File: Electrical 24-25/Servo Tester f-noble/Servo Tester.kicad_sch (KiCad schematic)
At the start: 5 parts, among them SW1 RotaryEncoder_Switch, U1 AP2205-33Y-13, U2 ATtiny404-SS, U3 PCF8551ATT_AJ, U4 VIM-878-DP-FC-S-LV

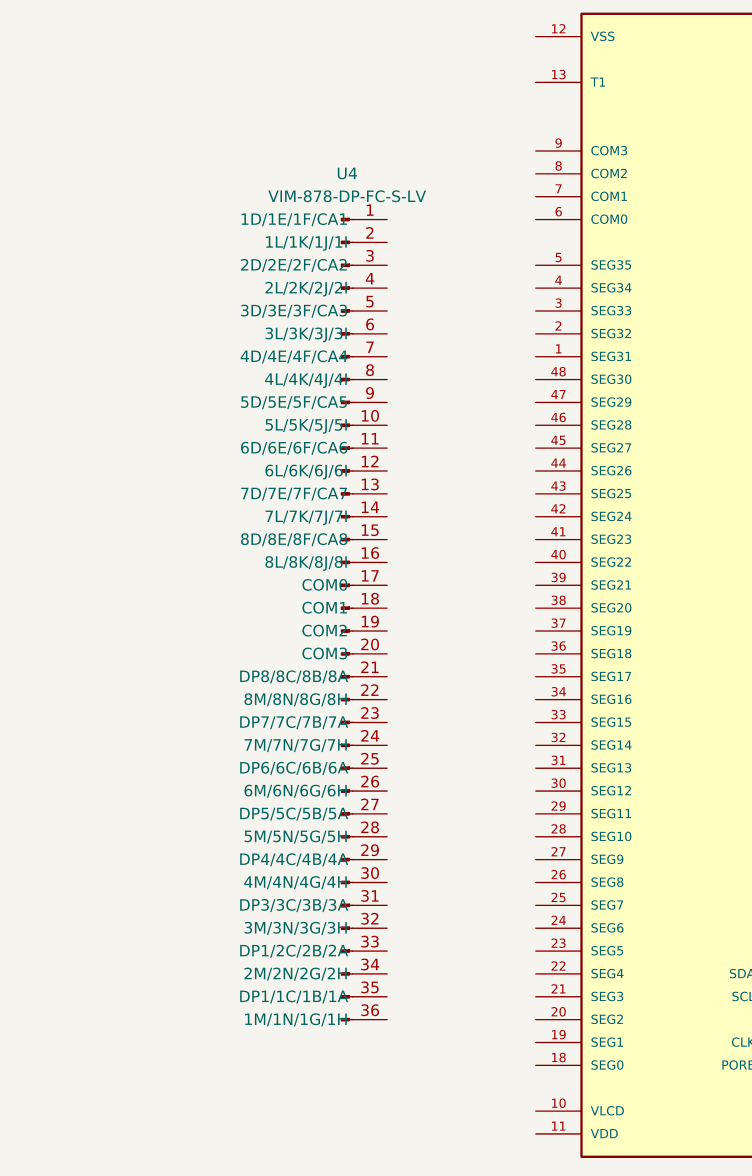
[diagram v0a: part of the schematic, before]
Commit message: added some led wires
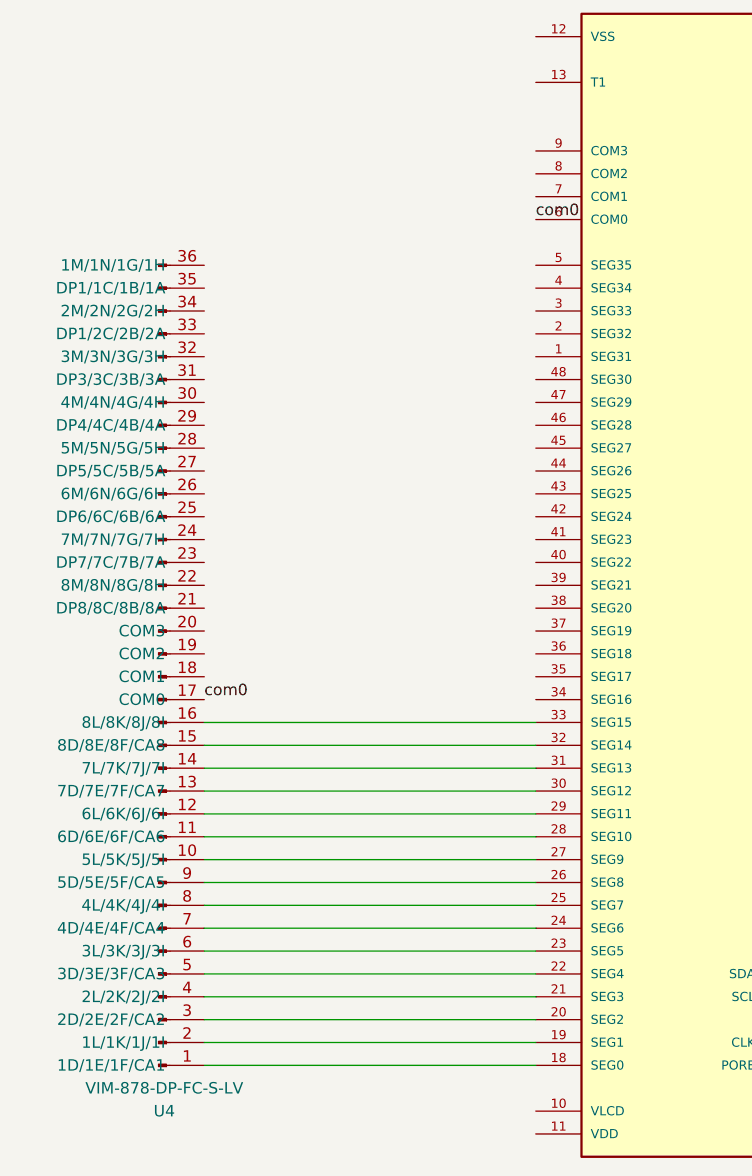
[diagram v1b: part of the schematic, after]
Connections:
- net at U4.1 (1D/1E/1F/CA1): now also U3.18 (SEG0)
- net at U4.10 (5L/5K/5J/5I): now also U3.27 (SEG9)
- net at U4.11 (6D/6E/6F/CA6): now also U3.28 (SEG10)
- net at U4.12 (6L/6K/6J/6I): now also U3.29 (SEG11)
- net at U4.13 (7D/7E/7F/CA7): now also U3.30 (SEG12)
- net at U4.14 (7L/7K/7J/7I): now also U3.31 (SEG13)
- net at U4.15 (8D/8E/8F/CA8): now also U3.32 (SEG14)
- net at U4.16 (8L/8K/8J/8I): now also U3.33 (SEG15)
- net com0: now reaches U4.17 (COM0)
- net com0: now also U3.6 (COM0)
- net at U4.2 (1L/1K/1J/1I): now also U3.19 (SEG1)
- net at U4.3 (2D/2E/2F/CA2): now also U3.20 (SEG2)
- net at U4.4 (2L/2K/2J/2I): now also U3.21 (SEG3)
- net at U4.5 (3D/3E/3F/CA3): now also U3.22 (SEG4)
- net at U4.6 (3L/3K/3J/3I): now also U3.23 (SEG5)
- net at U4.7 (4D/4E/4F/CA4): now also U3.24 (SEG6)
- net at U4.8 (4L/4K/4J/4I): now also U3.25 (SEG7)
- net at U4.9 (5D/5E/5F/CA5): now also U3.26 (SEG8)
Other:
- moved on the sheet: U4
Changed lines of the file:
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@@
+	(wire
+		(pts
+			(xy 34.29 152.4) (xy 71.12 152.4)
+		)
+		(stroke
+			(width 0)
+			(type default)
+		)
+	)
 	(wire
 		(pts
@@
 	(wire
 		(pts
+			(xy 34.29 149.86) (xy 71.12 149.86)
+		)
+		(stroke
+			(width 0)
+			(type default)
+		)
+	)
+	(wire
+		(pts
 			(xy 119.38 81.28) (xy 125.73 81.28)
 		)
@@
 	(wire
 		(pts
+			(xy 34.29 142.24) (xy 71.12 142.24)
+		)
+		(stroke
+			(width 0)
+			(type default)
+		)
+	)
+	(wire
+		(pts
 			(xy 107.95 88.9) (xy 133.35 88.9)
 		)
@@
 	(wire
 		(pts
+			(xy 34.29 165.1) (xy 71.12 165.1)
+		)
+		(stroke
+			(width 0)
+			(type default)
+		)
+	)
+	(wire
+		(pts
 			(xy 140.97 101.6) (xy 133.35 101.6)
 		)
@@
 	(wire
 		(pts
+			(xy 34.29 137.16) (xy 71.12 137.16)
+		)
+		(stroke
+			(width 0)
+			(type default)
+		)
+	)
+	(wire
+		(pts
 			(xy 133.35 148.59) (xy 138.43 148.59)
 		)
@@
 	(wire
 		(pts
+			(xy 34.29 170.18) (xy 71.12 170.18)
+		)
+		(stroke
+			(width 0)
+			(type default)
+		)
+	)
+	(wire
+		(pts
+			(xy 34.29 132.08) (xy 71.12 132.08)
+		)
+		(stroke
+			(width 0)
+			(type default)
+		)
+	)
+	(wire
+		(pts
+			(xy 34.29 162.56) (xy 71.12 162.56)
+		)
+		(stroke
+			(width 0)
+			(type default)
+		)
+	)
+	(wire
+		(pts
+			(xy 34.29 157.48) (xy 71.12 157.48)
+		)
+		(stroke
+			(width 0)
+			(type default)
+		)
+	)
+	(wire
+		(pts
+			(xy 34.29 139.7) (xy 71.12 139.7)
+		)
+		(stroke
+			(width 0)
+			(type default)
+		)
+	)
+	(wire
+		(pts
 			(xy 140.97 81.28) (xy 140.97 101.6)
 		)
@@
 	(wire
 		(pts
+			(xy 34.29 160.02) (xy 71.12 160.02)
+		)
+		(stroke
+			(width 0)
+			(type default)
+		)
+	)
+	(wire
+		(pts
 			(xy 133.35 148.59) (xy 133.35 154.94)
 		)
@@
 	(wire
 		(pts
+			(xy 34.29 167.64) (xy 71.12 167.64)
+		)
+		(stroke
+			(width 0)
+			(type default)
+		)
+	)
+	(wire
+		(pts
+			(xy 34.29 154.94) (xy 71.12 154.94)
+		)
+		(stroke
+			(width 0)
+			(type default)
+		)
+	)
+	(wire
+		(pts
+			(xy 34.29 134.62) (xy 71.12 134.62)
+		)
+		(stroke
+			(width 0)
+			(type default)
+		)
+	)
+	(wire
+		(pts
+			(xy 34.29 144.78) (xy 71.12 144.78)
+		)
+		(stroke
+			(width 0)
+			(type default)
+		)
+	)
+	(wire
+		(pts
 			(xy 119.38 69.85) (xy 119.38 81.28)
 		)
@@
 		)
 	)
-	(label "-VBATT"
-		(at 138.43 148.59 0)
+	(wire
+		(pts
+			(xy 34.29 147.32) (xy 71.12 147.32)
+		)
+		(stroke
+			(width 0)
+			(type default)
+		)
+	)
+	(label "com0"
+		(at 34.29 129.54 0)
 		(fields_autoplaced yes)
 		(effects
@@
 		)
 	)
+	(label "-VBATT"
+		(at 138.43 148.59 0)
+		(fields_autoplaced yes)
+		(effects
+			(font
+				(size 1.27 1.27)
+			)
+			(justify left bottom)
+		)
+	)
 	(label "+VBATT"
 		(at 119.38 69.85 0)
+		(fields_autoplaced yes)
+		(effects
+			(font
+				(size 1.27 1.27)
+			)
+			(justify left bottom)
+		)
+	)
+	(label "com0"
+		(at 71.12 76.2 0)
 		(fields_autoplaced yes)
 		(effects
@@
 	(symbol
 		(lib_id "servo_tester_onboarding:VIM-878-DP")
-		(at 49.53 119.38 0)
+		(at 29.21 127 0)
+		(mirror x)
 		(unit 1)
 		(exclude_from_sim no)
@@
 		(dnp no)
 		(property "Reference" "U4"
-			(at 50.165 71.12 0)
+			(at 29.845 175.26 0)
 			(effects
 				(font
@@
 		)
 		(property "Value" "VIM-878-DP-FC-S-LV"
-			(at 50.165 73.66 0)
+			(at 29.845 172.72 0)
 			(effects
 				(font
@@
 		)
 		(property "Footprint" ""
-			(at 49.53 119.38 0)
+			(at 29.21 127 0)
 			(effects
 				(font
@@
 		)
 		(property "Datasheet" "https://mm.digikey.com/Volume0/opasdata/d220001/medias/docus/693/VIM-878.pdf"
-			(at 49.53 120.015 0)
+			(at 29.21 126.365 0)
 			(effects
 				(font
@@
 		)
 		(property "Description" ""
-			(at 49.53 119.38 0)
+			(at 29.21 127 0)
 			(effects
 				(font
@@
 		)
 		(property "Digi" "https://www.digikey.com/en/products/detail/varitronix/VIM-878-DP-FC-S-LV/1118603"
-			(at 51.435 122.555 0)
-			(effects
-				(font
+			(at 31.115 123.825 0)
+			(effects
+				(font

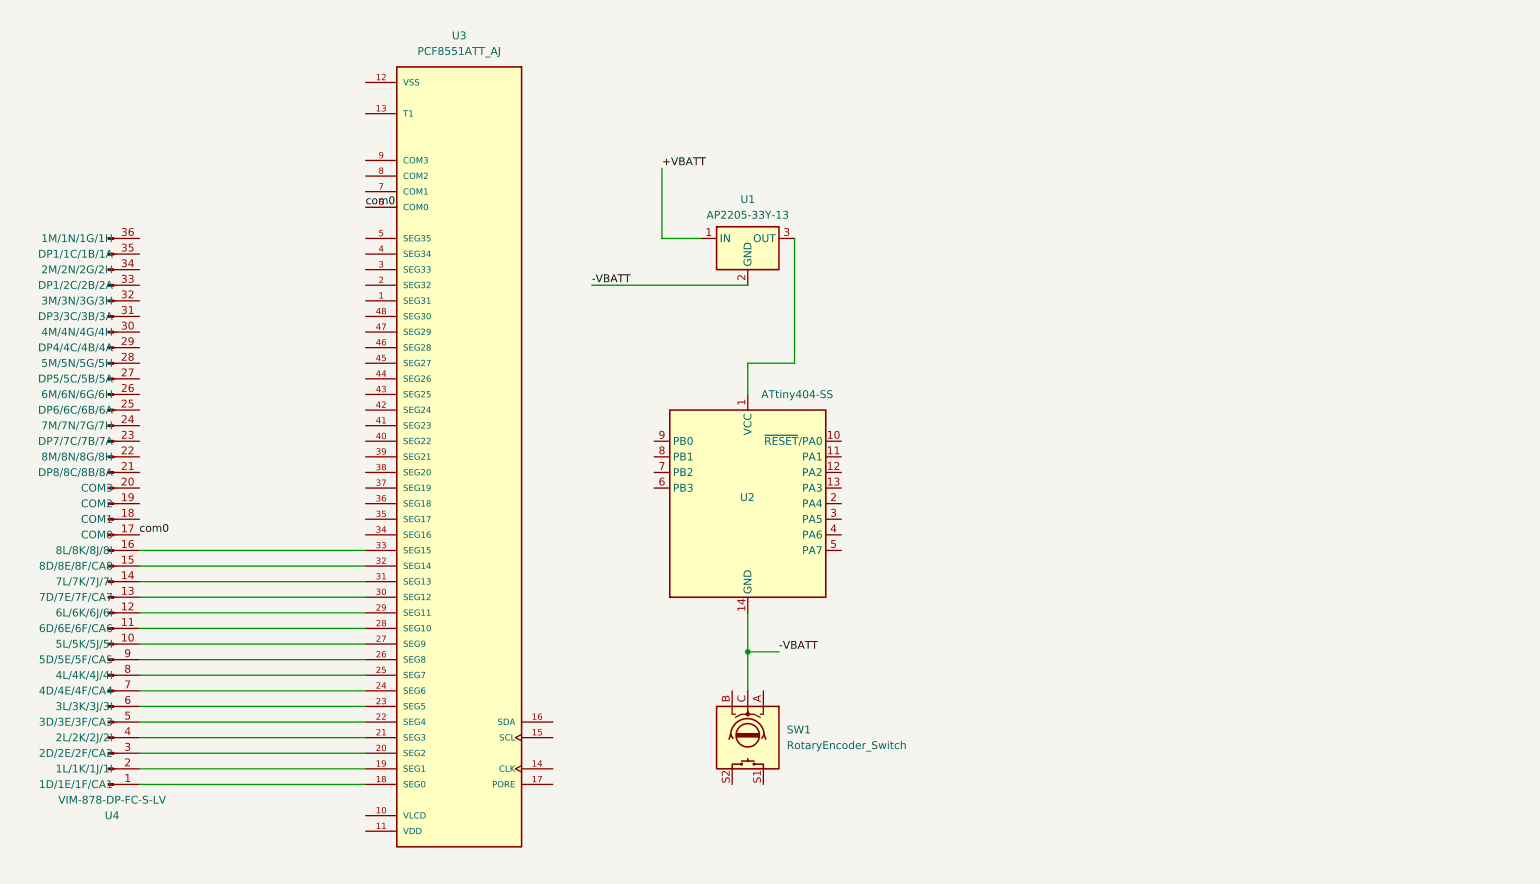
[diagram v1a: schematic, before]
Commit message: The board is almost done
Mostly done except that I'm not sure about the filter and I need to know whether to connect the LCD as I2C or otherwise
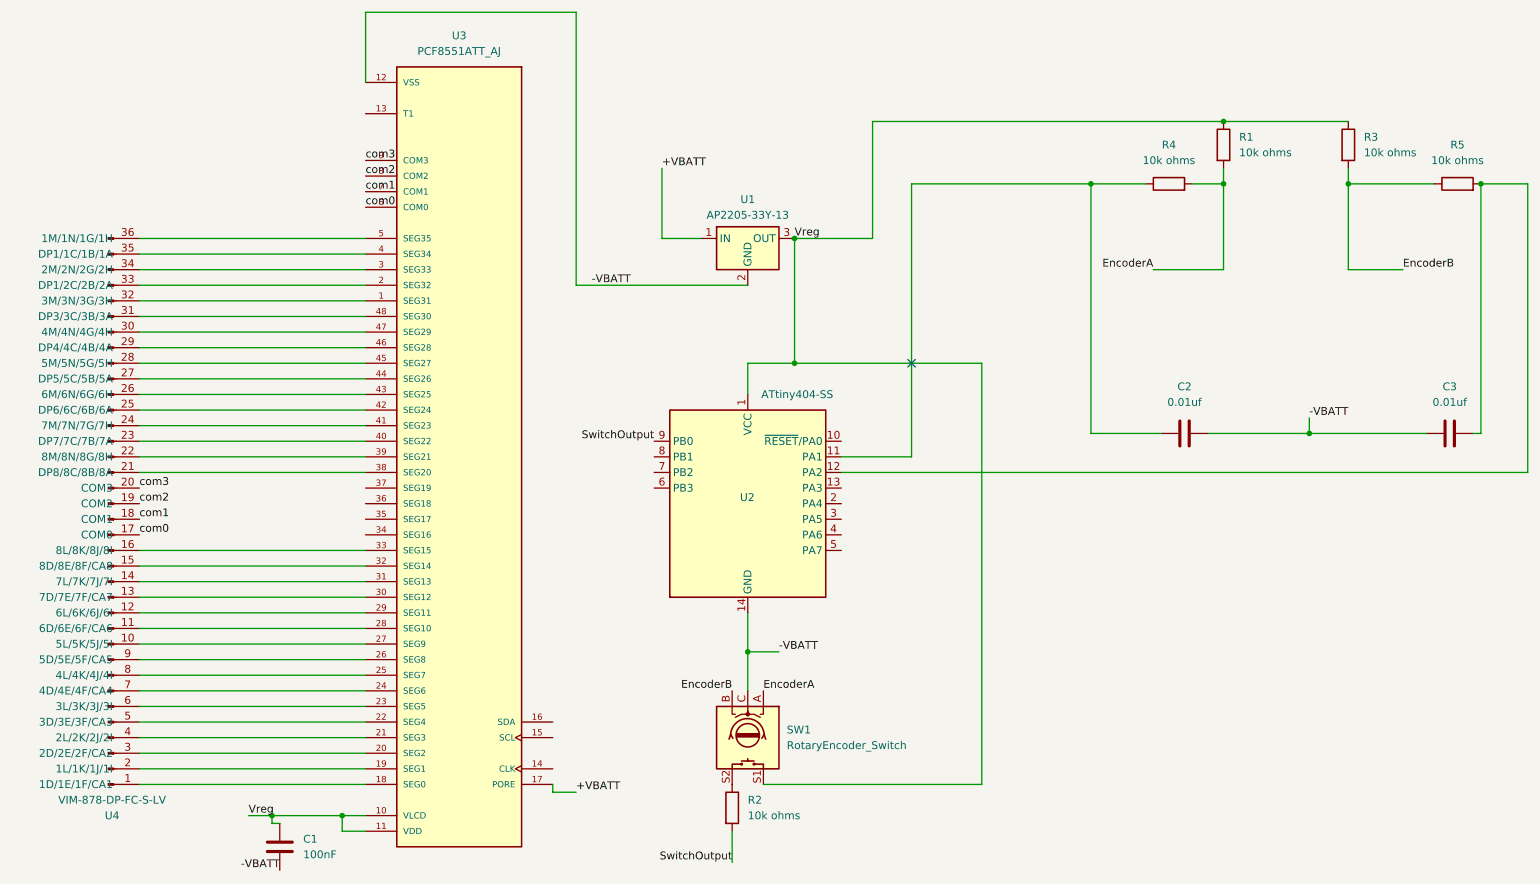
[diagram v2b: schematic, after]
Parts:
- added C1: 100nF, symbol Device:C
- added C2, C3: 0.01uf, symbol Device:C
- added R1, R2, R3, R4, R5: 10k ohms, symbol Device:R
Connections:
- net +VBATT: now also U3.17 (PORE)
- net -VBATT: now also U3.12 (VSS), C1.1, C2.2, C3.1
- net Vreg: now reaches U1.3 (OUT), U2.1 (VCC)
- net Vreg: now also SW1.S1, U3.10 (VLCD), U3.11 (VDD), C1.2, R1.1, R3.1
- net at U2.11 (PA1): now also C2.1, R4.1
- net at U2.12 (PA2): now also C3.2, R5.2
- net SwitchOutput: now reaches U2.9 (PB0)
- net SwitchOutput: now also R2.2
- net com1: now reaches U4.18 (COM1)
- net com1: now also U3.7 (COM1)
- net com2: now reaches U4.19 (COM2)
- net com2: now also U3.8 (COM2)
- net com3: now reaches U4.20 (COM3)
- net com3: now also U3.9 (COM3)
- net at U4.21 (DP8/8C/8B/8A): now also U3.38 (SEG20)
- net at U4.22 (8M/8N/8G/8H): now also U3.39 (SEG21)
- net at U4.23 (DP7/7C/7B/7A): now also U3.40 (SEG22)
- net at U4.24 (7M/7N/7G/7H): now also U3.41 (SEG23)
- net at U4.25 (DP6/6C/6B/6A): now also U3.42 (SEG24)
- net at U4.26 (6M/6N/6G/6H): now also U3.43 (SEG25)
- net at U4.27 (DP5/5C/5B/5A): now also U3.44 (SEG26)
- net at U4.28 (5M/5N/5G/5H): now also U3.45 (SEG27)
- net at U4.29 (DP4/4C/4B/4A): now also U3.46 (SEG28)
- net at U4.30 (4M/4N/4G/4H): now also U3.47 (SEG29)
- net at U4.31 (DP3/3C/3B/3A): now also U3.48 (SEG30)
- net at U4.32 (3M/3N/3G/3H): now also U3.1 (SEG31)
- net at U4.33 (DP1/2C/2B/2A): now also U3.2 (SEG32)
- net at U4.34 (2M/2N/2G/2H): now also U3.3 (SEG33)
- net at U4.35 (DP1/1C/1B/1A): now also U3.4 (SEG34)
- net at U4.36 (1M/1N/1G/1H): now also U3.5 (SEG35)
- net EncoderA: now reaches SW1.A
- net EncoderA: now also R1.2, R4.2
- net EncoderB: now reaches SW1.B
- net EncoderB: now also R3.2, R5.1
- net at SW1.S2: now also R2.1
- no-connect marks 0 -> 1
